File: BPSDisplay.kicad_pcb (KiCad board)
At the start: 2 copper layers, 85 x 56 mm, 59 parts, among them J1 SWD, J3 CAN_Out, J4 CAN_Out, J5 CarPowerConnector, J6 CAN_LogicAnalyzer, J7 SPI0_LogicAnalyzer, J8 GEN_LogicAnalyzer, J9 USART_LogicAnalyzer, P1 Conn_02x20_Odd_Even, SW1 Reset, U1 STM32F413RHTx, U2 ADM3055E, U3 CDSOT23-T24CAN, U6 PDS1-S12-S5, U7 NCP1117-3.3_SOT223, Y1 8M

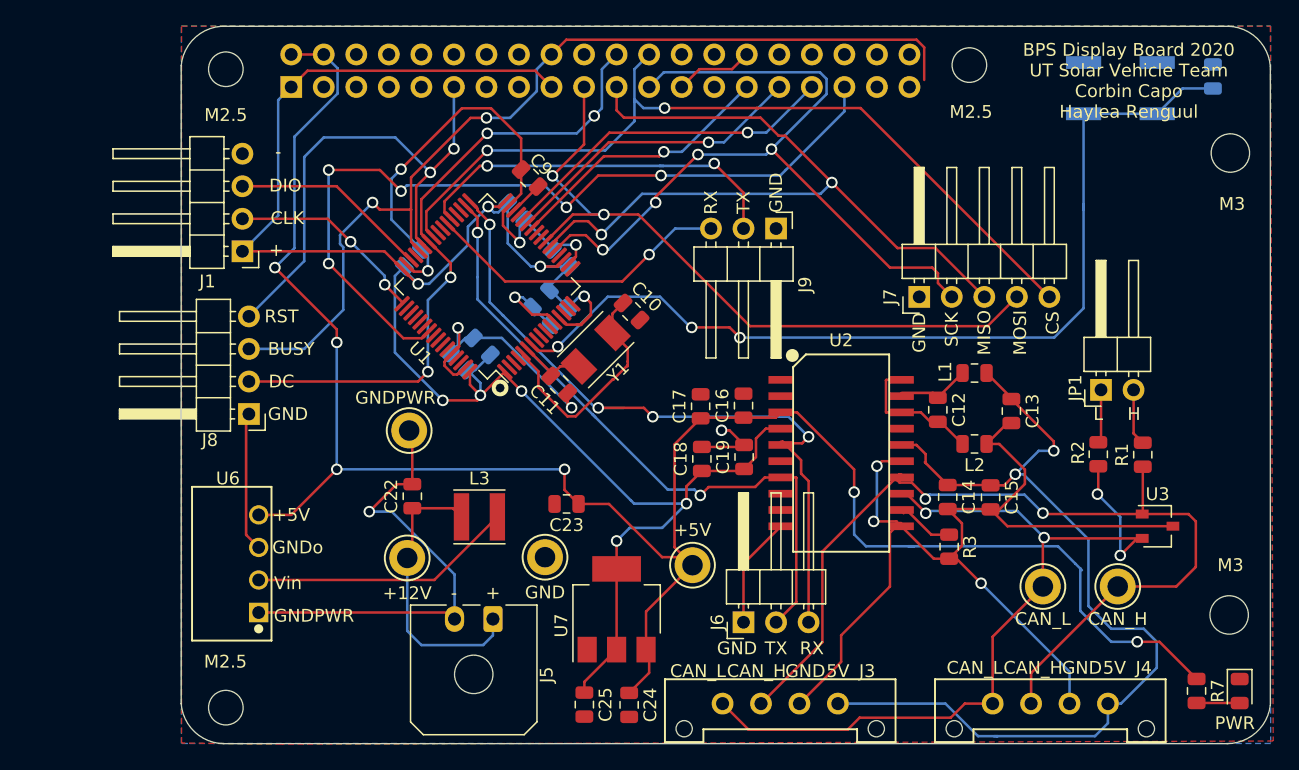
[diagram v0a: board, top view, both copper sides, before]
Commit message: Updated footprints, re-routed traces
Changed logical analyzer footprints to vertical, changed 2x20 connector footprint back to the original footprint, changed CAN headers to vertical footprints.
Grouped components better so logic analyzer pins are closer to their corresponding pins on the microcontroller. Re-did traces accordingly.
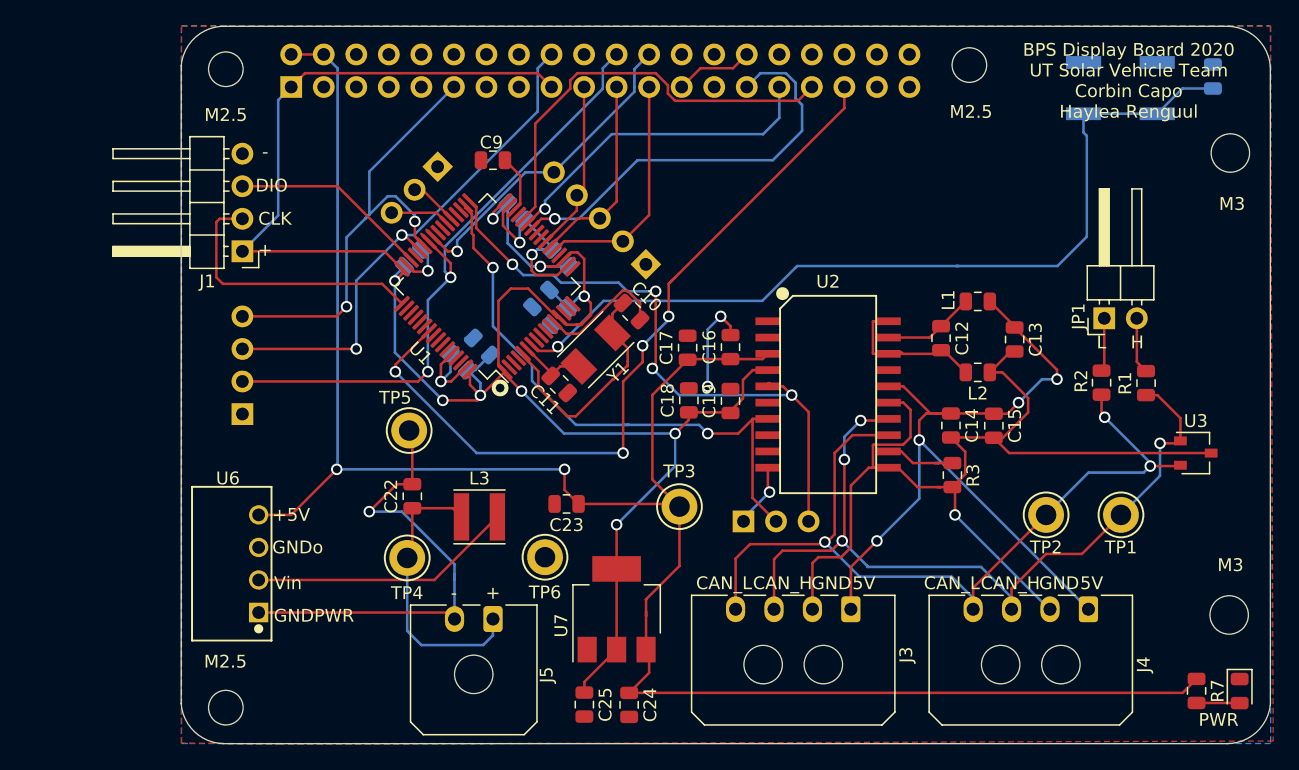
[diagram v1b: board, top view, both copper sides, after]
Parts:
- removed CAN_H: CAN_H, TestPoint:TestPoint_Keystone_5005-5009_Compact
- removed CAN_L: CAN_L, TestPoint:TestPoint_Keystone_5005-5009_Compact
- removed J6: CAN_LogicAnalyzer, Connector_PinHeader_2.54mm:PinHeader_1x03_P2.54mm_Horizontal
- removed J7: SPI0_LogicAnalyzer, Connector_PinHeader_2.54mm:PinHeader_1x05_P2.54mm_Horizontal
- removed J8: GEN_LogicAnalyzer, Connector_PinHeader_2.54mm:PinHeader_1x04_P2.54mm_Horizontal
- removed J9: USART_LogicAnalyzer, Connector_PinHeader_2.54mm:PinHeader_1x03_P2.54mm_Horizontal
- added CAN: CAN_LogicAnalyzer, Connector_PinHeader_2.54mm:PinHeader_1x03_P2.54mm_Vertical, B.Cu at (239.9, 143.7)
- added GEN: GEN_LogicAnalyzer, Connector_PinHeader_2.54mm:PinHeader_1x04_P2.54mm_Vertical, B.Cu at (200.8, 135.3)
- added SPIO: SPI0_LogicAnalyzer, Connector_PinHeader_2.54mm:PinHeader_1x05_P2.54mm_Vertical, B.Cu at (232.3, 123.6)
- added TP1: CAN_H, TestPoint:TestPoint_Keystone_5005-5009_Compact, F.Cu at (269.3, 143.1)
- added TP2: CAN_L, TestPoint:TestPoint_Keystone_5005-5009_Compact, F.Cu at (263.5, 143.1)
- added UART: USART_LogicAnalyzer, Connector_PinHeader_2.54mm:PinHeader_1x03_P2.54mm_Vertical, B.Cu at (216.0, 116.0)
- J3, J4: footprint UTSVT_Connectors:Molex_MicroFit3.0_1x4xP3.00mm_PolarizingPeg_Vertical -> Connector_Molex:Molex_Micro-Fit_3.0_43650-0400_1x04_P3.00mm_Horizontal
- P1: footprint Connector_PinSocket_2.54mm:PinSocket_2x20_P2.54mm_Horizontal -> Connector_PinSocket_2.54mm:PinSocket_2x20_P2.54mm_Vertical
- moved J4 7.52 mm to (266.8, 150.5)
- moved J3 7.44 mm to (248.3, 150.5)
- moved U3 6.44 mm to (275.2, 138.3)
- moved L2 5.59 mm to (258.2, 132.0)
- moved R1 5.59 mm to (271.3, 132.9)
- moved C15 5.59 mm to (259.4, 136.2)
- moved L1 5.59 mm to (258.2, 126.5)
- moved R2 5.59 mm to (267.8, 132.8)
- moved C12 5.59 mm to (255.3, 129.3)
- moved C14 5.59 mm to (256.1, 136.2)
- moved R3 5.59 mm to (256.2, 140.0)
- moved C13 5.59 mm to (261.0, 129.4)
- moved JP1 5.59 mm to (268.0, 127.8)
- moved TP3 4.68 mm to (234.9, 142.5)
- moved C16 4.68 mm to (238.9, 130.0)
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- renumbered +5V to TP3, +12V to TP4, GNDPWR to TP5, GND to TP6
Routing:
- net /GPIO9(SPI0_MISO): track 61.5 -> 15.6 mm, vias 2 -> 0
- net /GPIO11(SPI0_SCK): track 62.5 -> 18.5 mm, vias 4 -> 0
- net /GPIO10(SPI0_MOSI): track 55.4 -> 13.3 mm, vias 2 -> 0
- net GND: track 102.1 -> 60.4 mm, vias 8 -> 7
- net /GPIO8(SPI0_CE_N): track 66.0 -> 26.0 mm, vias 2 -> 1
- net /GPIO24(GEN5): track 76.6 -> 42.0 mm
- net /USART6_TX: track 30.3 -> 4.63 mm, vias 2 -> 0
- net /USART6_RX: track 24.2 -> 4.77 mm, vias 1 -> 0
- net Net-(C13-Pad1): track 74.1 -> 61.7 mm, vias 2 -> 4
- net /GPIO5: track 21.3 -> 32.8 mm
- net /CAN/CAN_H: track 74.2 -> 64.3 mm, vias 2 -> 4
- net /CAN2_RX: track 57.5 -> 49.1 mm
- net /CAN2_TX: track 52.7 -> 45.6 mm
- net /GPIO13: track 26.8 -> 33.2 mm, vias 1 -> 0
- net /SWCLK: track 15.7 -> 21.9 mm, vias 2 -> 0
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
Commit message: Fixed traces
Got rid of traces with right angles, made labels on CAN headers vertical, made traces neater, added logo and picture of Dr. Hallock on back
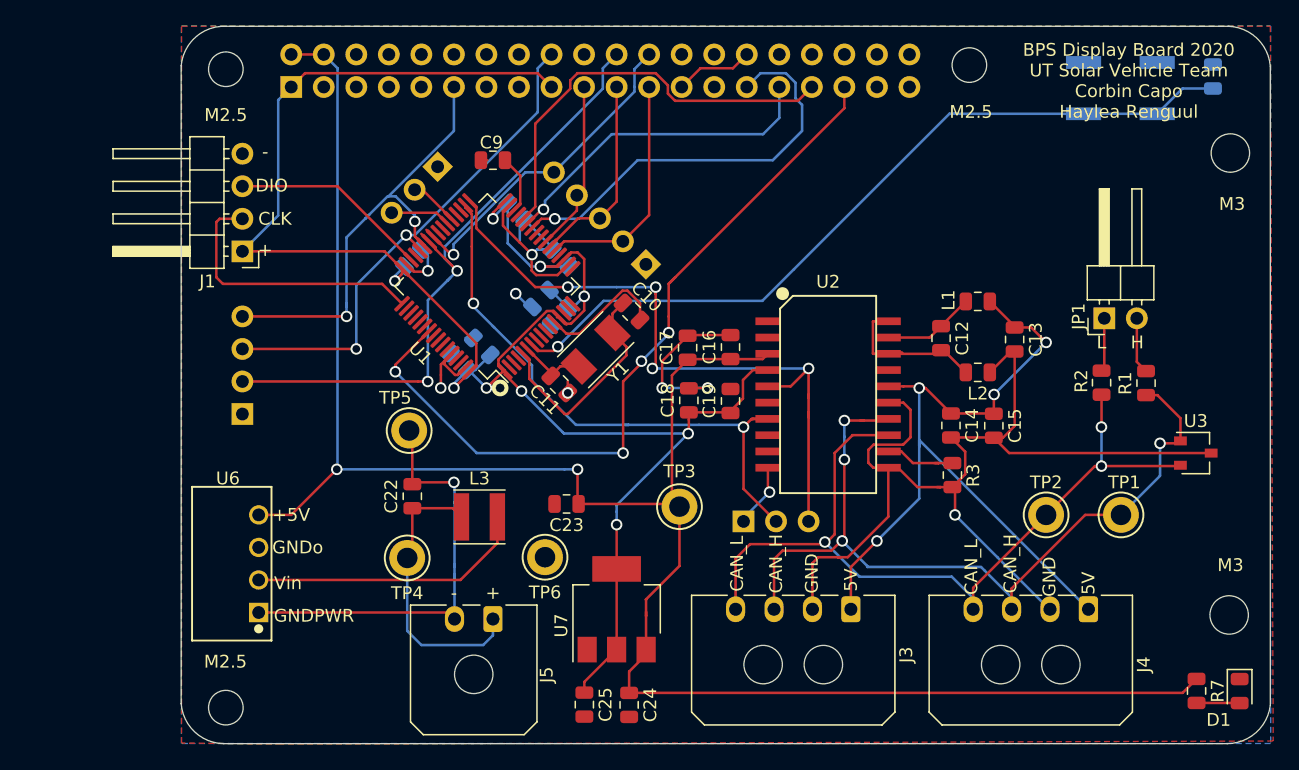
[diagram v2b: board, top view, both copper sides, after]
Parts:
- added LOGO1: Logo_Placeholder, UTSVT_Special:UTSVT_Logo_Symbol, B.Cu at (230.5, 154.8)
- added LOGO2: Logo_Placeholder, UTSVT_Special:Hallock_Image_Tiny, B.Cu at (257.9, 120.0)
- renumbered PWR to D1, CAN to J6, SPIO to J7, GEN to J8, UART to J9
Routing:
- net GND: track 60.4 -> 69.0 mm, vias 7 -> 8
- net /NRST: track 68.0 -> 62.3 mm
- net +3V3: track 164.8 -> 159.3 mm
- net /CAN2_RX: track 49.1 -> 53.4 mm
- net GNDPWR: track 36.7 -> 34.1 mm
- net /GPIO24(GEN5): track 42.0 -> 39.8 mm
- net /CAN/CAN_L: track 66.8 -> 65.2 mm
- net /GPIO17(GEN0): track 39.1 -> 37.6 mm
- net Net-(L3-Pad2): track 20.7 -> 21.9 mm
- net /CAN/CAN_H: track 64.3 -> 65.3 mm
- net /GPIO25(GEN6): track 49.9 -> 50.8 mm
- net Net-(C13-Pad1): track 61.7 -> 60.8 mm
- net Net-(C10-Pad1): track 19.4 -> 18.6 mm

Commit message: Aligning components, editing text
Aligned connectors on the south end to the edge of the board, edited text for title of the board, rotated JP1 90 degrees clockwise, and removed the trace appendage on C5.
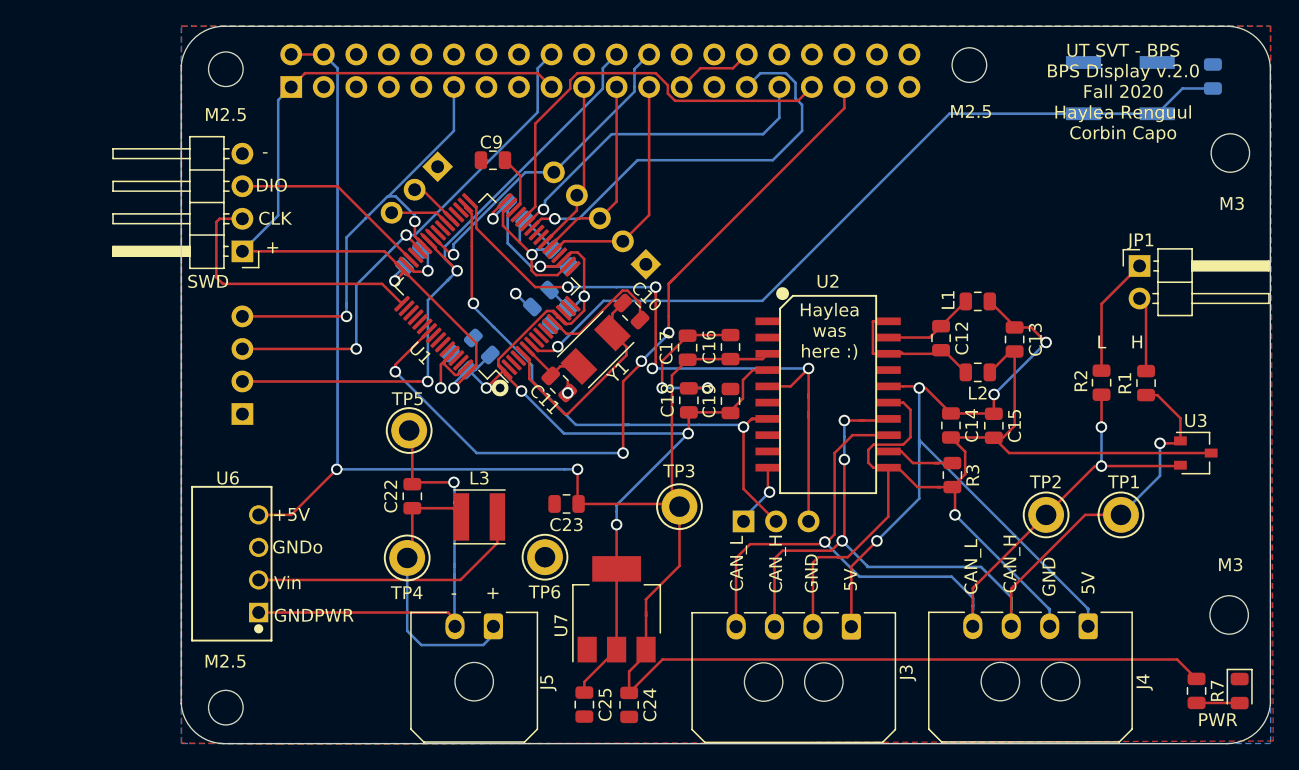
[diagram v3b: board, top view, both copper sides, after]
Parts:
- moved JP1 4.93 mm to (270.8, 123.7), turned to 0 degrees
- moved J3 1.36 mm to (248.3, 151.9)
- moved J4 1.33 mm to (266.8, 151.8)
- moved J5 0.57 mm to (220.4, 151.8)
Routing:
- net /CAN/TERM_L: track 4.18 -> 9.70 mm
- net /CAN/CAN_H: track 65.3 -> 69.8 mm
- net /CAN/CAN_L: track 65.2 -> 69.6 mm
- net Net-(C13-Pad2): track 81.5 -> 84.3 mm
- net Net-(C13-Pad1): track 60.8 -> 63.5 mm
- net /CAN/TERM_H: track 4.42 -> 5.88 mm
- net +5V: track 154.3 -> 155.6 mm
- net GND: track 69.0 -> 68.4 mm
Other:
- board text added: "CAN"
- board text added: "GEN"
- board text added: "Haylea was here :)"
- board text added: "PWR"
- board text added: "SPIO"
- board text added: "SWD"
- board text added: "UART"
- board text added: "UT SVT - BPS BPS Display v.2.0 Fall 2020 Haylea Renguul Corbin Capo"
- board text removed: "BPS Display Board 2020 UT Solar Vehicle Team Corbin Capo Haylea Renguul"

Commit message: Fixed labels
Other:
- board text added: "UTSVT - BPS BPS Display v.2.0 Fall 2020 Haylea Renguul"
- board text removed: "UT SVT - BPS BPS Display v.2.0 Fall 2020 Haylea Renguul Corbin Capo"
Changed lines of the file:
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@@
     (tags resistor)
     (attr smd)
-    (fp_text reference R7 (at 0 -1.65 90) (layer F.SilkS)
+    (fp_text reference R7 (at -0.12192 1.45542 90) (layer F.SilkS)
       (effects (font (size 1 1) (thickness 0.15)))
     )
@@
     (tags diode)
     (attr smd)
-    (fp_text reference D1 (at 2.25044 1.64338 180) (layer F.SilkS) hide
+    (fp_text reference D1 (at -0.15494 1.77546 270) (layer F.SilkS)
       (effects (font (size 1 1) (thickness 0.15)))
     )
@@
     (effects (font (size 1 1) (thickness 0.15)))
   )
-  (gr_text "UT SVT - BPS\nBPS Display v.2.0\nFall 2020\nHaylea Renguul\nCorbin Capo" (at 269.51472 110.12962) (layer F.SilkS)
+  (gr_text "UTSVT - BPS\nBPS Display v.2.0\nFall 2020\nHaylea Renguul" (at 269.51472 110.12962) (layer F.SilkS)
     (effects (font (size 1 1) (thickness 0.15)))
   )
@@
   (segment (start 239.054999 108.278001) (end 236.514999 108.278001) (width 0.2) (layer F.Cu) (net 3))
   (segment (start 240.132 107.201) (end 239.054999 108.278001) (width 0.2) (layer F.Cu) (net 3))
-  (via (at 222.098 125.87) (size 0.9) (drill 0.6) (layers F.Cu B.Cu) (net 3))
   (segment (start 223.403587 126.913913) (end 223.141913 126.913913) (width 0.2) (layer B.Cu) (net 3))
   (segment (start 223.141913 126.913913) (end 222.098 125.87) (width 0.2) (layer B.Cu) (net 3))
@@
   (segment (start 216.256 132.22) (end 216.256 133.224997) (width 0.2) (layer F.Cu) (net 3))
   (via (at 216.244997 133.236) (size 0.9) (drill 0.6) (layers F.Cu B.Cu) (net 3))
+  (via (at 222.098 125.87) (size 0.9) (drill 0.6) (layers F.Cu B.Cu) (net 3))
   (segment (start 223.368161 120.757879) (end 224.09804 120.028) (width 0.2) (layer F.Cu) (net 4) (status 10))
   (via (at 225.146 120.028) (size 0.9) (drill 0.6) (layers F.Cu B.Cu) (net 4))

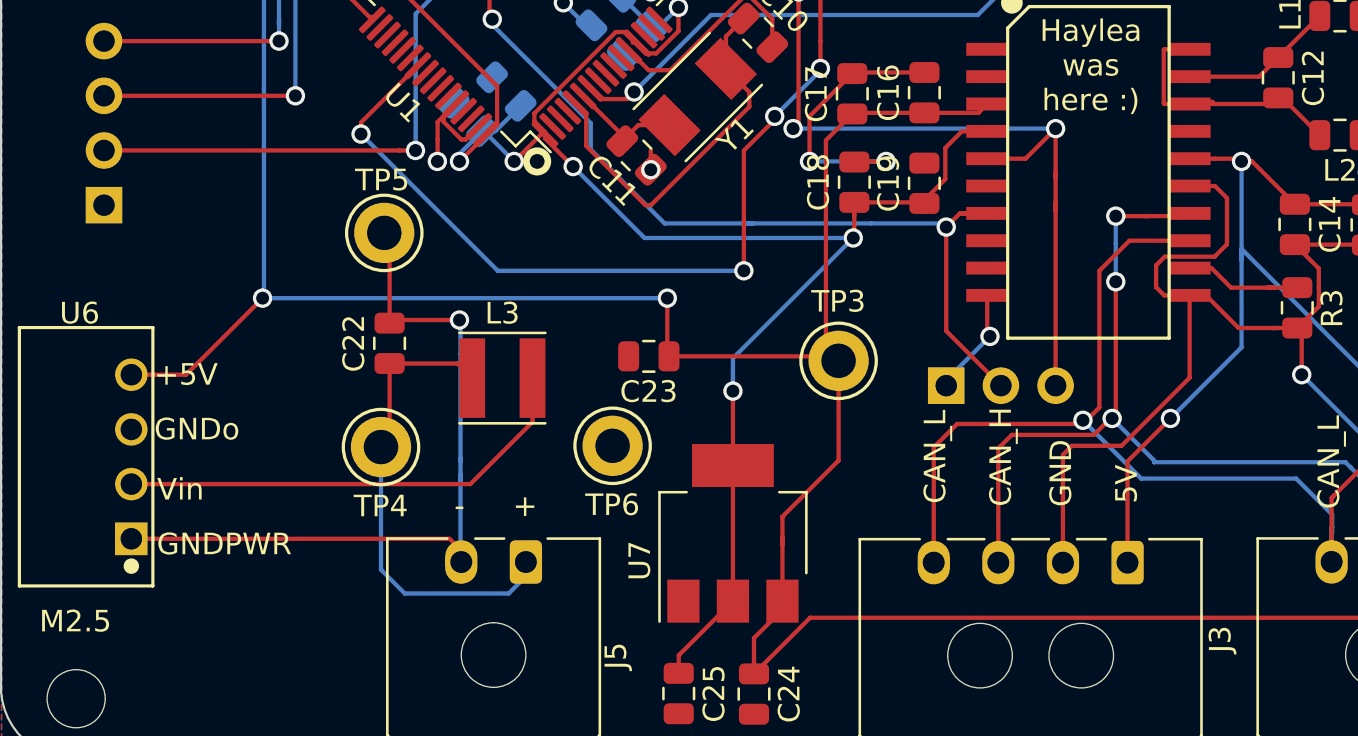
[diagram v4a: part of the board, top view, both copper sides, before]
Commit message: Moved traces to avoid shorts
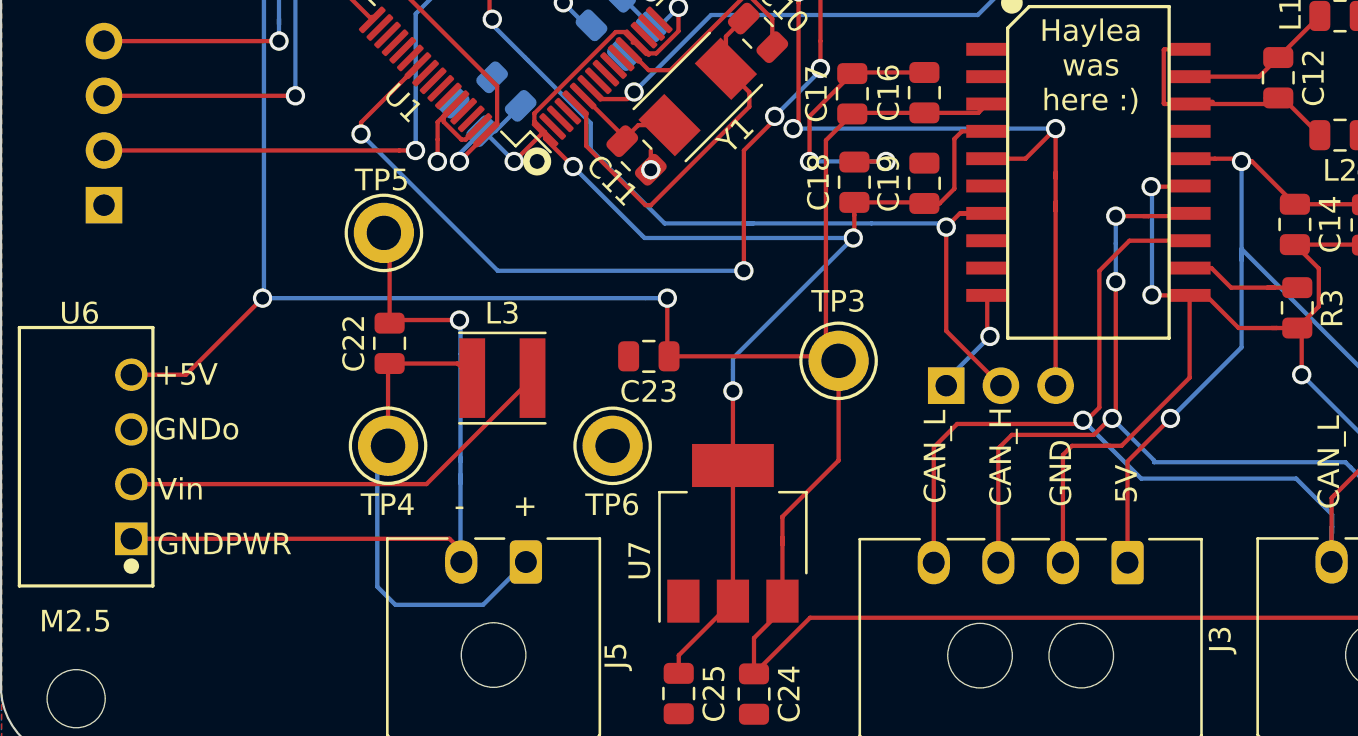
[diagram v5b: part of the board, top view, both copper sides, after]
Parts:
- moved TP4 0.33 mm to (214.0, 146.4)
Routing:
- net Net-(C13-Pad2): track 84.3 -> 82.4 mm, vias 1 -> 3
- net +12V: track 23.1 -> 24.5 mm
- net Net-(L3-Pad2): track 21.9 -> 20.7 mm
- net +3V3: track 159.3 -> 159.9 mm
